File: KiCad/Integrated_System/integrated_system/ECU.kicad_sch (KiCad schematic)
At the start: 50 parts, among them J1 Jack-DC, J2 Fan 1, J3 Fan 2, J4 Fan 3, Q1 TN0702N3, Q2 TN0702N3, Q3 TN0702N3, SW1 SW_SPDT, SW2 SW_SPDT, SW3 SW_Push, U1 SGP30, U2 BME680, U4 Mini360 DC to DC Buck Convert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, U5 SCD30

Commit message: changed wire
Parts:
- renumbered D6 to D1, D5 to D10, D4 to D11, D7 to D2, D8 to D3, D9 to D7, D10 to D8, D11 to D9, Q1 to Q2, Q2 to Q3, Q3 to Q4, R9 to R1, R12 to R10, R13 to R11, R14 to R12, R4 to R13, R5 to R14, R10 to R2, R11 to R3, R6 to R4, R7 to R5, R8 to R6, U4 to U1

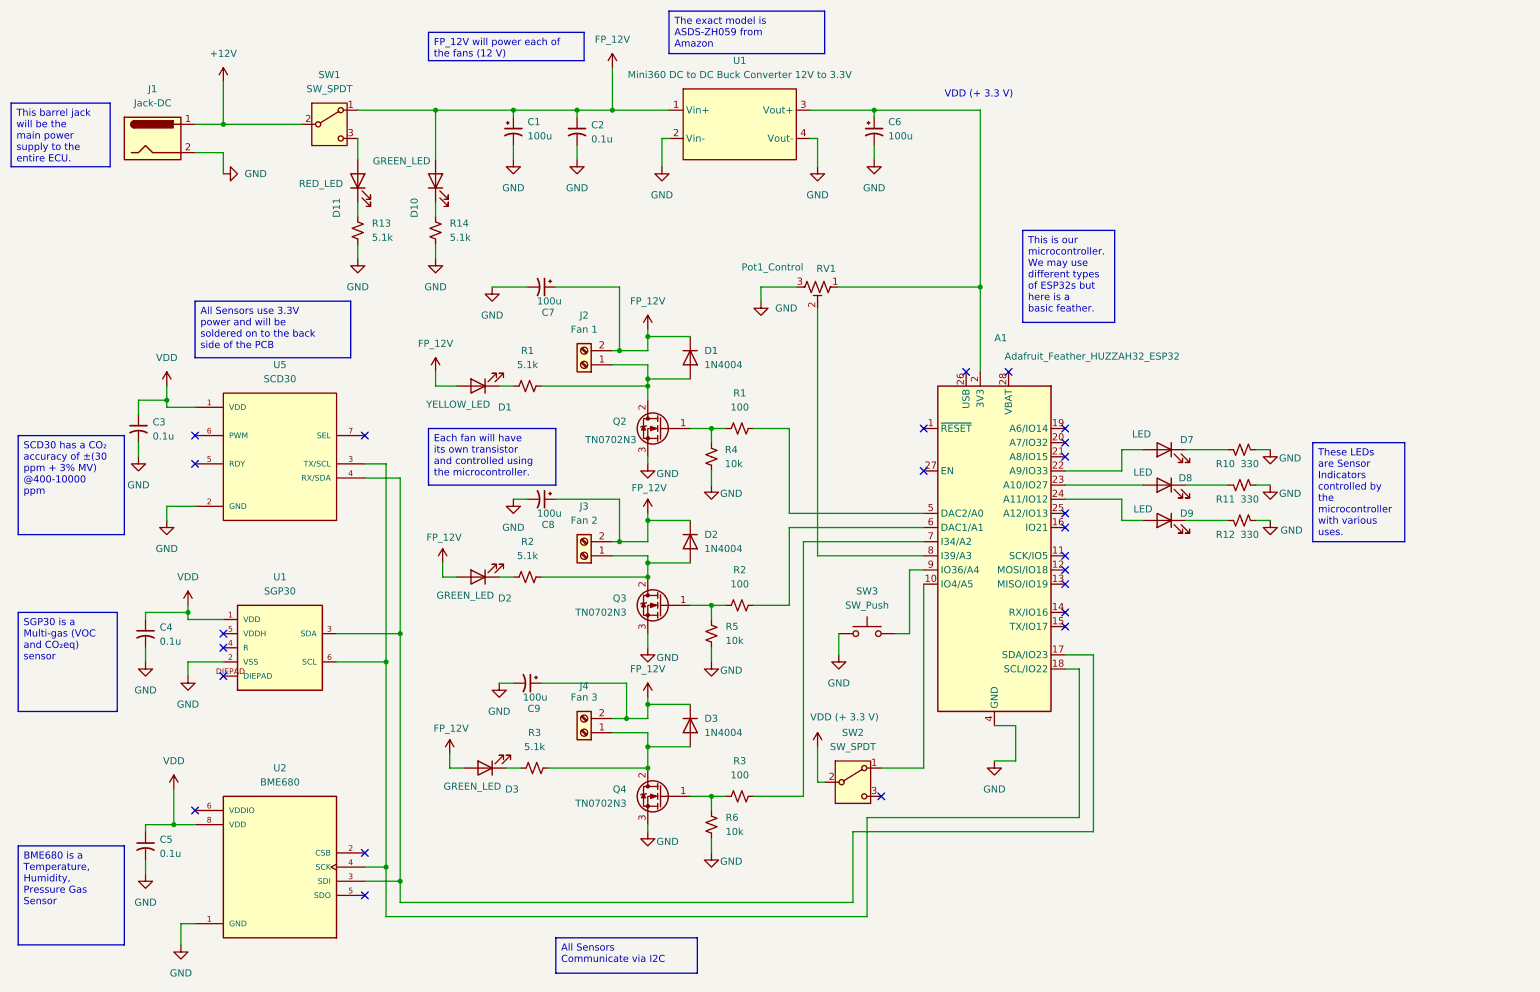
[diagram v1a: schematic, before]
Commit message: Replaced the transistors to BSS138
BSS138 is SMD type
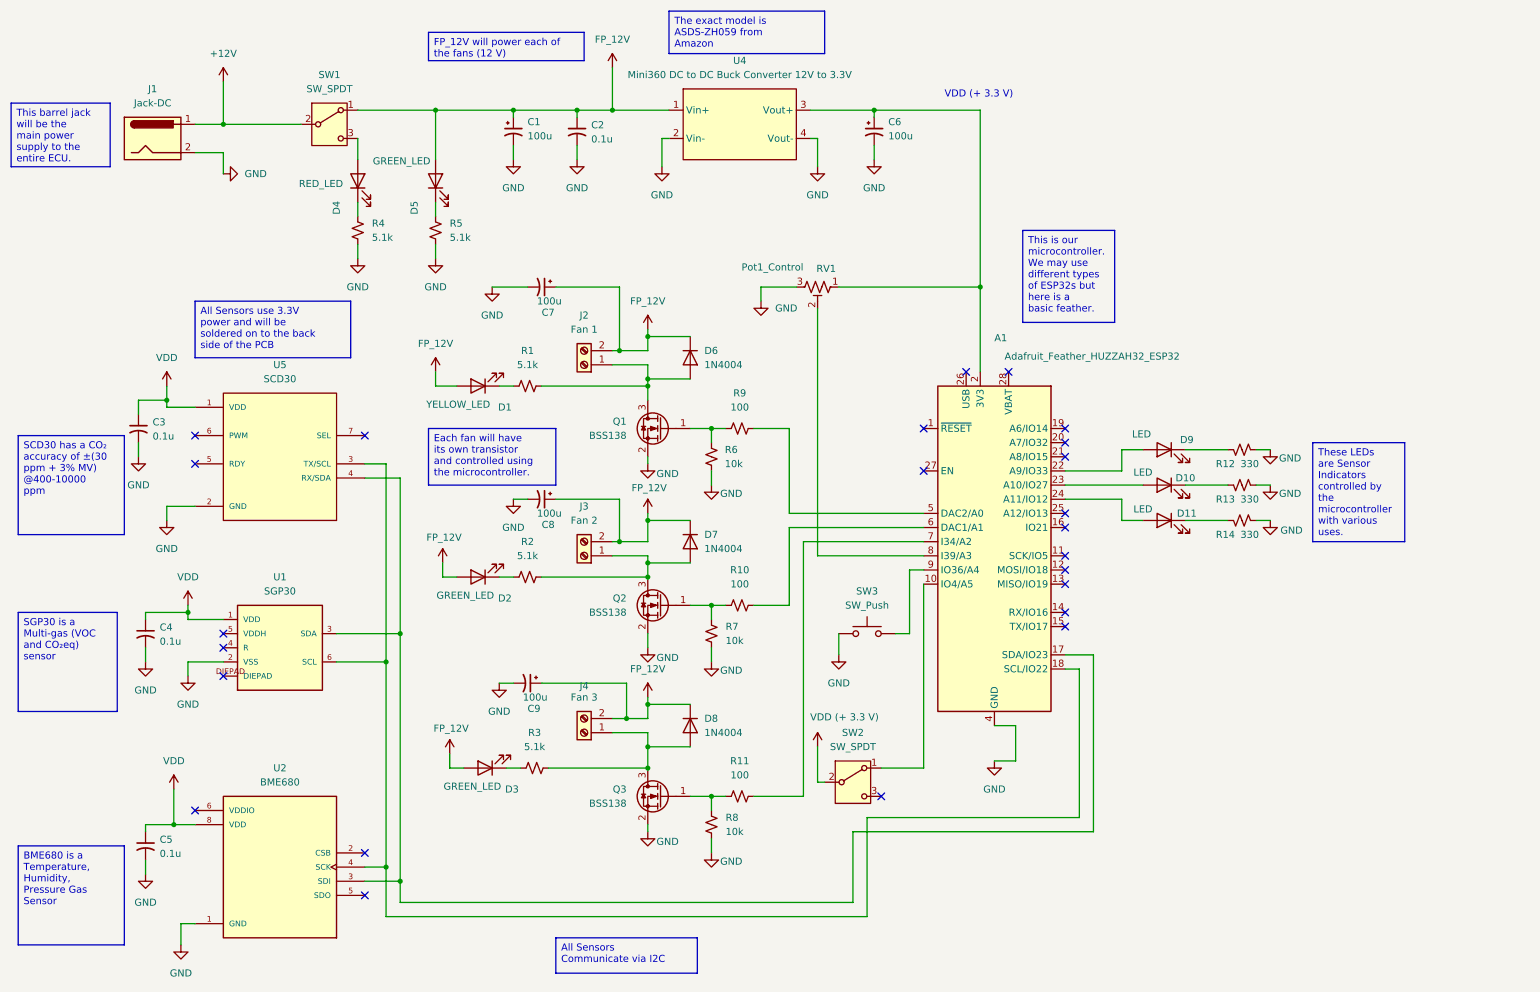
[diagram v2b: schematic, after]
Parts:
- removed Q2, Q3, Q4: TN0702N3, TN0702N3-G:TRANS_TP2104N3-G, symbol Transistor_FET:IRLB8721PBF
- added Q1, Q2, Q3: BSS138, Package_TO_SOT_SMD:SOT-23_Handsoldering, symbol Transistor_FET:BSS138
- renumbered D8 to D10, D9 to D11, D11 to D4, D10 to D5, D1 to D6, D2 to D7, D3 to D8, D7 to D9, R2 to R10, R3 to R11, R10 to R12, R11 to R13, R12 to R14, R13 to R4, R14 to R5, R4 to R6, R5 to R7, R6 to R8, R1 to R9, U1 to U4
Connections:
- net GND: now also Q1.2 (S), Q2.2 (S), Q3.2 (S)
- net at R6.2, R9.1: now also Q1.1 (G)
- net at D8.2 (A), J4.1 (Pin_1), R3.2: now also Q3.3 (D)
- net at D6.2 (A), J2.1 (Pin_1), R1.2: now also Q1.3 (D)
- net at D7.2 (A), J3.1 (Pin_1), R2.2: now also Q2.3 (D)
- net at R10.1, R7.2: now also Q2.1 (G)
- net at R11.1, R8.2: now also Q3.1 (G)

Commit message: updates
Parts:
- removed U5: SCD30, SCD30:MODULE_SCD30, symbol SCD30:SCD30
- added U3: SCD30, SCD30:MODULE_SCD30, symbol SCD30:SCD30
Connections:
- net GND: now also U3.2 (GND)
- net VDD: now also U3.1 (VDD)
- net at A1.17 (SDA/IO23), U1.3 (SDA), U2.3 (SDI): now also U3.4 (RX/SDA)
- net at A1.18 (SCL/IO22), U1.6 (SCL), U2.4 (SCK): now also U3.3 (TX/SCL)
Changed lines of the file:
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@@
 	(wire
 		(pts
-			(xy 193.04 148.59) (xy 189.23 148.59)
-		)
-		(stroke
-			(width 0)
-			(type default)
-		)
-	)
-	(wire
-		(pts
 			(xy 41.91 160.02) (xy 45.72 160.02)
 		)
@@
 	(wire
 		(pts
-			(xy 193.04 142.24) (xy 193.04 148.59)
+			(xy 189.23 142.24) (xy 189.23 148.59)
 		)
 		(stroke
@@
 	(wire
 		(pts
-			(xy 193.04 142.24) (xy 189.23 142.24)
-		)
-		(stroke
-			(width 0)
-			(type default)
-		)
-	)
-	(wire
-		(pts
 			(xy 40.64 102.87) (xy 40.64 105.41)
 		)
@@
 	)
 	(symbol
+		(lib_id "SCD30:SCD30")
+		(at 60.96 95.25 0)
+		(mirror y)
+		(unit 1)
+		(exclude_from_sim no)
+		(in_bom yes)
+		(on_board yes)
+		(dnp no)
+		(fields_autoplaced yes)
+		(property "Reference" "U3"
+			(at 60.96 77.47 0)
+			(effects
+				(font
+					(size 1.27 1.27)
+				)
+			)
+		)
+		(property "Value" "SCD30"
+			(at 60.96 80.01 0)
+			(effects
+				(font
+					(size 1.27 1.27)
+				)
+			)
+		)
+		(property "Footprint" "SCD30:MODULE_SCD30"
+			(at 60.96 95.25 0)
+			(effects
+				(font
+					(size 1.27 1.27)
+				)
+				(justify bottom)
+				(hide yes)
+			)
+		)
+		(property "Datasheet" ""
+			(at 60.96 95.25 0)
+			(effects
+				(font
+					(size 1.27 1.27)
+				)
+				(hide yes)
+			)
+		)
+		(property "Description" ""
+			(at 60.96 95.25 0)
+			(effects
+				(font
+					(size 1.27 1.27)
+				)
+				(hide yes)
+			)
+		)
+		(property "PARTREV" "D1"
+			(at 60.96 95.25 0)
+			(effects
+				(font
+					(size 1.27 1.27)
+				)
+				(justify bottom)
+				(hide yes)
+			)
+		)
+		(property "STANDARD" "Manufacturer Recommendations"
+			(at 60.96 95.25 0)
+			(effects
+				(font
+					(size 1.27 1.27)
+				)
+				(justify bottom)
+				(hide yes)
+			)
+		)
+		(property "MAXIMUM_PACKAGE_HEIGHT" "7.0mm"
+			(at 60.96 95.25 0)
+			(effects
+				(font
+					(size 1.27 1.27)
+				)
+				(justify bottom)
+				(hide yes)
+			)
+		)
+		(property "MANUFACTURER" "Sensirion"
+			(at 60.96 95.25 0)
+			(effects
+				(font
+					(size 1.27 1.27)
+				)
+				(justify bottom)
+				(hide yes)
+			)
+		)
+		(pin "7"
+		)
+		(pin "4"
+		)
+		(pin "5"
+		)
+		(pin "1"
+		)
+		(pin "6"
+		)
+		(pin "2"
+		)
+		(pin "3"
+		)
+		(instances
+			(project ""
+				(path "/68e66ac2-e6c8-4149-aa8e-681ce71fac5d"
+					(reference "U3")
+					(unit 1)
+				)
+			)
+		)
+	)
+	(symbol
 		(lib_id "Transistor_FET:BSS138")
 		(at 129.54 88.9 0)
@@
 					(unit 1)
 				)
-			)
-		)
-	)
-	(symbol
-		(lib_id "SCD30:SCD30")
-		(at 60.96 95.25 0)
-		(mirror y)
-		(unit 1)
-		(exclude_from_sim no)
-		(in_bom yes)
-		(on_board yes)
-		(dnp no)
-		(property "Reference" "U5"
-			(at 60.96 77.47 0)
-			(effects
-				(font
-					(size 1.27 1.27)
-				)
-			)
-		)
-		(property "Value" "SCD30"
-			(at 60.96 80.01 0)
-			(effects
-				(font
-					(size 1.27 1.27)
-				)
-			)
-		)
-		(property "Footprint" "SCD30:MODULE_SCD30"
-			(at 60.96 95.25 0)
-			(effects
-				(font
-					(size 1.27 1.27)
-				)
-				(justify bottom)
-				(hide yes)
-			)
-		)
-		(property "Datasheet" ""
-			(at 60.96 95.25 0)
-			(effects
-				(font
-					(size 1.27 1.27)
-				)
-				(hide yes)
-			)
-		)
-		(property "Description" ""
-			(at 60.96 95.25 0)
-			(effects
-				(font
-					(size 1.27 1.27)
-				)
-				(hide yes)
-			)
-		)
-		(property "MF" "Sensirion AG"
-			(at 60.96 95.25 0)
-			(effects
-				(font
-					(size 1.27 1.27)
-				)
-				(justify bottom)
-				(hide yes)
-			)
-		)
-		(property "MAXIMUM_PACKAGE_HEIGHT" "7.0mm"
-			(at 60.96 95.25 0)
-			(effects
-				(font
-					(size 1.27 1.27)
-				)
-				(justify bottom)
-				(hide yes)
-			)
-		)
-		(property "Package" "None"
-			(at 60.96 95.25 0)
-			(effects
-				(font
-					(size 1.27 1.27)
-				)
-				(justify bottom)
-				(hide yes)
-			)
-		)
-		(property "Price" "None"
-			(at 60.96 95.25 0)
-			(effects
-				(font
-					(size 1.27 1.27)
-				)
-				(justify bottom)
-				(hide yes)
-			)
-		)
-		(property "Check_prices" "https://www.snapeda.com/parts/SCD30/Sensirion/view-part/?ref=eda"
-			(at 60.96 95.25 0)
-			(effects
-				(font
-					(size 1.27 1.27)
-				)
-				(justify bottom)
-				(hide yes)
-			)
-		)
-		(property "STANDARD" "Manufacturer Recommendations"
-			(at 60.96 95.25 0)
-			(effects
-				(font
-					(size 1.27 1.27)
-				)
-				(justify bottom)
-				(hide yes)
-			)
-		)
-		(property "PARTREV" "D1"
-			(at 60.96 95.25 0)
-			(effects
-				(font
-					(size 1.27 1.27)
-				)
-				(justify bottom)
-				(hide yes)
-			)
-		)
-		(property "SnapEDA_Link" "https://www.snapeda.com/parts/SCD30/Sensirion/view-part/?ref=snap"
-			(at 60.96 95.25 0)
-			(effects
-				(font
-					(size 1.27 1.27)
-				)
-				(justify bottom)
-				(hide yes)
-			)
-		)
-		(property "MP" "SCD30"
-			(at 60.96 95.25 0)
-			(effects
-				(font
-					(size 1.27 1.27)
-				)
-				(justify bottom)
-				(hide yes)
-			)
-		)
-		(property "Purchase-URL" "https://www.snapeda.com/api/url_track_click_mouser/?unipart_id=2779194&manufacturer=Sensirion AG&part_name=SCD30&search_term=None"
-			(at 60.96 95.25 0)
-			(effects
-				(font
-					(size 1.27 1.27)
-				)
-				(justify bottom)
-				(hide yes)
-			)
-		)
-		(property "Description_1" "Carbon Dioxide (CO2), Humidity, Temperature Sensor I2C, Modbus, PWM"
-			(at 60.96 95.25 0)
-			(effects
-				(font
-					(size 1.27 1.27)
-				)
-				(justify bottom)
-				(hide yes)
-			)
-		)
-		(property "Availability" "In Stock"
-			(at 60.96 95.25 0)
-			(effects
-				(font
-					(size 1.27 1.27)
-				)
-				(justify bottom)
-				(hide yes)
-			)
-		)
-		(property "MANUFACTURER" "Sensirion"
-			(at 60.96 95.25 0)
-			(effects
-				(font
-					(size 1.27 1.27)
-				)
-				(justify bottom)
-				(hide yes)
-			)
-		)
-		(pin "2"
-		)
-		(pin "4"
-		)
-		(pin "7"
-		)
-		(pin "3"
-		)
-		(pin "5"
-		)
-		(pin "1"
-		)
-		(pin "6"
-		)
-		(instances
-			(project ""
-				(path "/68e66ac2-e6c8-4149-aa8e-681ce71fac5d"
-					(reference "U5")
-					(unit 1)
-				)
-			)
-			(project "integrated_system"
-				(path "/e09e0073-4b34-4087-926d-a963f587ec36/d64a58e5-7375-438d-b343-064b897cc797"
-					(reference "U?")
-					(unit 1)
-				)

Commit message: redesign v1.3
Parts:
- removed C7, C8, C9: 100u, Capacitor_SMD:CP_Elec_3x5.3, symbol Device:C_Polarized_Small_US
- added SW4: SW_Push, Button_Switch_THT:SW_PUSH_6mm, symbol Switch:SW_Push
- C1, C6: footprint Capacitor_SMD:CP_Elec_3x5.3 -> Capacitor_SMD:CP_Elec_6.3x7.7
- D10: value LED -> Yellow_LED
- D11: value LED -> Red_LED
- D9: value LED -> Green_LED
- J1: footprint Connector_BarrelJack:BarrelJack_CLIFF_FC681465S_SMT_Horizontal -> Connector_BarrelJack:BarrelJack_GCT_DCJ200-10-A_Horizontal
- RV1: footprint Potentiometer_THT:Potentiometer_Vishay_43_Horizontal -> Potentiometer_THT:Potentiometer_Bourns_3296W_Vertical
- SW1, SW2: footprint Button_Switch_THT:SW_DIP_SPSTx01_Slide_6.7x4.1mm_W7.62mm_P2.54mm_LowProfile -> switch_DM:switch_dm
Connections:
- net GND: now also SW4.1
- net at A1.25 (A12/IO13): now also SW4.2
- no-connect marks 24 -> 23
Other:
- moved on the sheet: A1, D1, D10, D11, D2, D3, D6, D7, D8, D9, J2, J3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

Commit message: Layout Complete
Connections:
- net +12V renamed +12V AC to DC wall adapter
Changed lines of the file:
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@@
 			)
 		)
-		(property "Value" "+12V"
+		(property "Value" "+12V AC to DC wall adapter"
 			(at 50.8 21.59 0)
 			(effects

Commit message: v1 Routing
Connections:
- net VDD (+ 3.3 V): now also A1.2 (3V3), C6.1, RV1.1, U4.3 (Vout+)
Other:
- note removed: "VDD (+ 3.3 V)"
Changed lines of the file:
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@@
 		(company "OSSEM")
 	)
-	(text "VDD (+ 3.3 V)"
-		(exclude_from_sim no)
-		(at 205.486 28.956 0)
-		(effects
-			(font
-				(size 1.27 1.27)
-			)
-		)
-	)
 	(text_box "These LEDs are Sensor Indicators controlled by the microcontroller with various uses."
 		(exclude_from_sim no)
@@
 	)
 	(junction
+		(at 205.74 31.75)
+		(diameter 0)
+		(color 0 0 0 0)
+	)
+	(junction
 		(at 135.89 113.03)
 		(diameter 0)
@@
 	(wire
 		(pts
+			(xy 205.74 27.94) (xy 205.74 31.75)
+		)
+		(stroke
+			(width 0)
+			(type default)
+		)
+	)
+	(wire
+		(pts
 			(xy 161.29 120.65) (xy 161.29 106.68)
 		)
@@
 					(unit 1)
 				)
+			)
+		)
+	)
+	(symbol
+		(lib_id "power:+12V")
+		(at 205.74 27.94 0)
+		(unit 1)
+		(exclude_from_sim no)
+		(in_bom yes)
+		(on_board yes)
+		(dnp no)
+		(property "Reference" "#PWR010"
+			(at 205.74 31.75 0)
+			(effects
+				(font
+					(size 1.27 1.27)
+				)
+				(hide yes)
+			)
+		)
+		(property "Value" "VDD (+ 3.3 V)"
+			(at 210.566 22.606 0)
+			(effects
+				(font
+					(size 1.27 1.27)
+				)
+			)
+		)
+		(property "Footprint" ""
+			(at 205.74 27.94 0)
+			(effects
+				(font
+					(size 1.27 1.27)
+				)
+				(hide yes)
+			)
+		)
+		(property "Datasheet" ""
+			(at 205.74 27.94 0)
+			(effects
+				(font
+					(size 1.27 1.27)
+				)
+				(hide yes)
+			)
+		)
+		(property "Description" "Power symbol creates a global label with name \"+12V\""
+			(at 205.74 27.94 0)
+			(effects
+				(font
+					(size 1.27 1.27)
+				)
+				(hide yes)
+			)
+		)
+		(pin "1"
+		)
+		(instances
+			(project "ECU"
+				(path "/68e66ac2-e6c8-4149-aa8e-681ce71fac5d"
+					(reference "#PWR010")
+					(unit 1)
+				)

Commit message: changes
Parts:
- added R15, R16: 4.7k, Resistor_SMD:R_1206_3216Metric_Pad1.30x1.75mm_HandSolder, symbol Device:R_Small_US
- R12, R13, R14: value 330 -> 1k
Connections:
- net VDD is gone; now on net VDD (+ 3.3 V): C3.1, C4.1, C5.1, U1.1 (VDD), U2.8 (VDD), U3.1 (VDD)
- net GND: now also D10.1 (K), D11.1 (K), D9.1 (K); no longer R12.1, R13.1, R14.1
- net VDD (+ 3.3 V): now also R15.1, R16.1
- net at R14.2: now also A1.24 (A11/IO12); no longer D11.1 (K)
- net at D11.2 (A): now also R14.1; no longer A1.24 (A11/IO12)
- net at A1.17 (SDA/IO23), U1.3 (SDA), U2.3 (SDI)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: now also R15.2
- net at A1.18 (SCL/IO22), U1.6 (SCL), U2.4 (SCK)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: now also R16.2
- net at R13.2: now also A1.23 (A10/IO27); no longer D10.1 (K)
- net at D10.2 (A): now also R13.1; no longer A1.23 (A10/IO27)
- net at R12.2: now also A1.22 (A9/IO33); no longer D9.1 (K)
- net at D9.2 (A): now also R12.1; no longer A1.22 (A9/IO33)
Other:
- note added: "include 4 pins i2c power"
- moved on the sheet: D10, D11, D9, R12, R13, R14
